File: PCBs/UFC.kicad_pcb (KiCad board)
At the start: 2 copper layers, 184.1 x 108 mm, 71 parts, among them J10 Conn_01x08_Male, J11 Conn_01x09_Male, J12 Conn_01x08_Male, J13 Conn_01x09_Male, J3 Power, J5 Matrix, J7 Driver output 2, J9 Conn_01x30_Male, SW1 SW_SPST, SW10 SW_SPST, SW11 SW_SPST, SW12 SW_SPST, SW13 SW_SPST, SW14 SW_SPST, SW15 SW_SPST, SW16 SW_SPST, SW17 SW_SPST, SW2 SW_SPST, SW3 SW_SPST, SW4 SW_SPST, SW5 SW_SPST, SW6 SW_SPST, SW7 SW_SPST, SW8 SW_SPST, SW9 SW_SPST

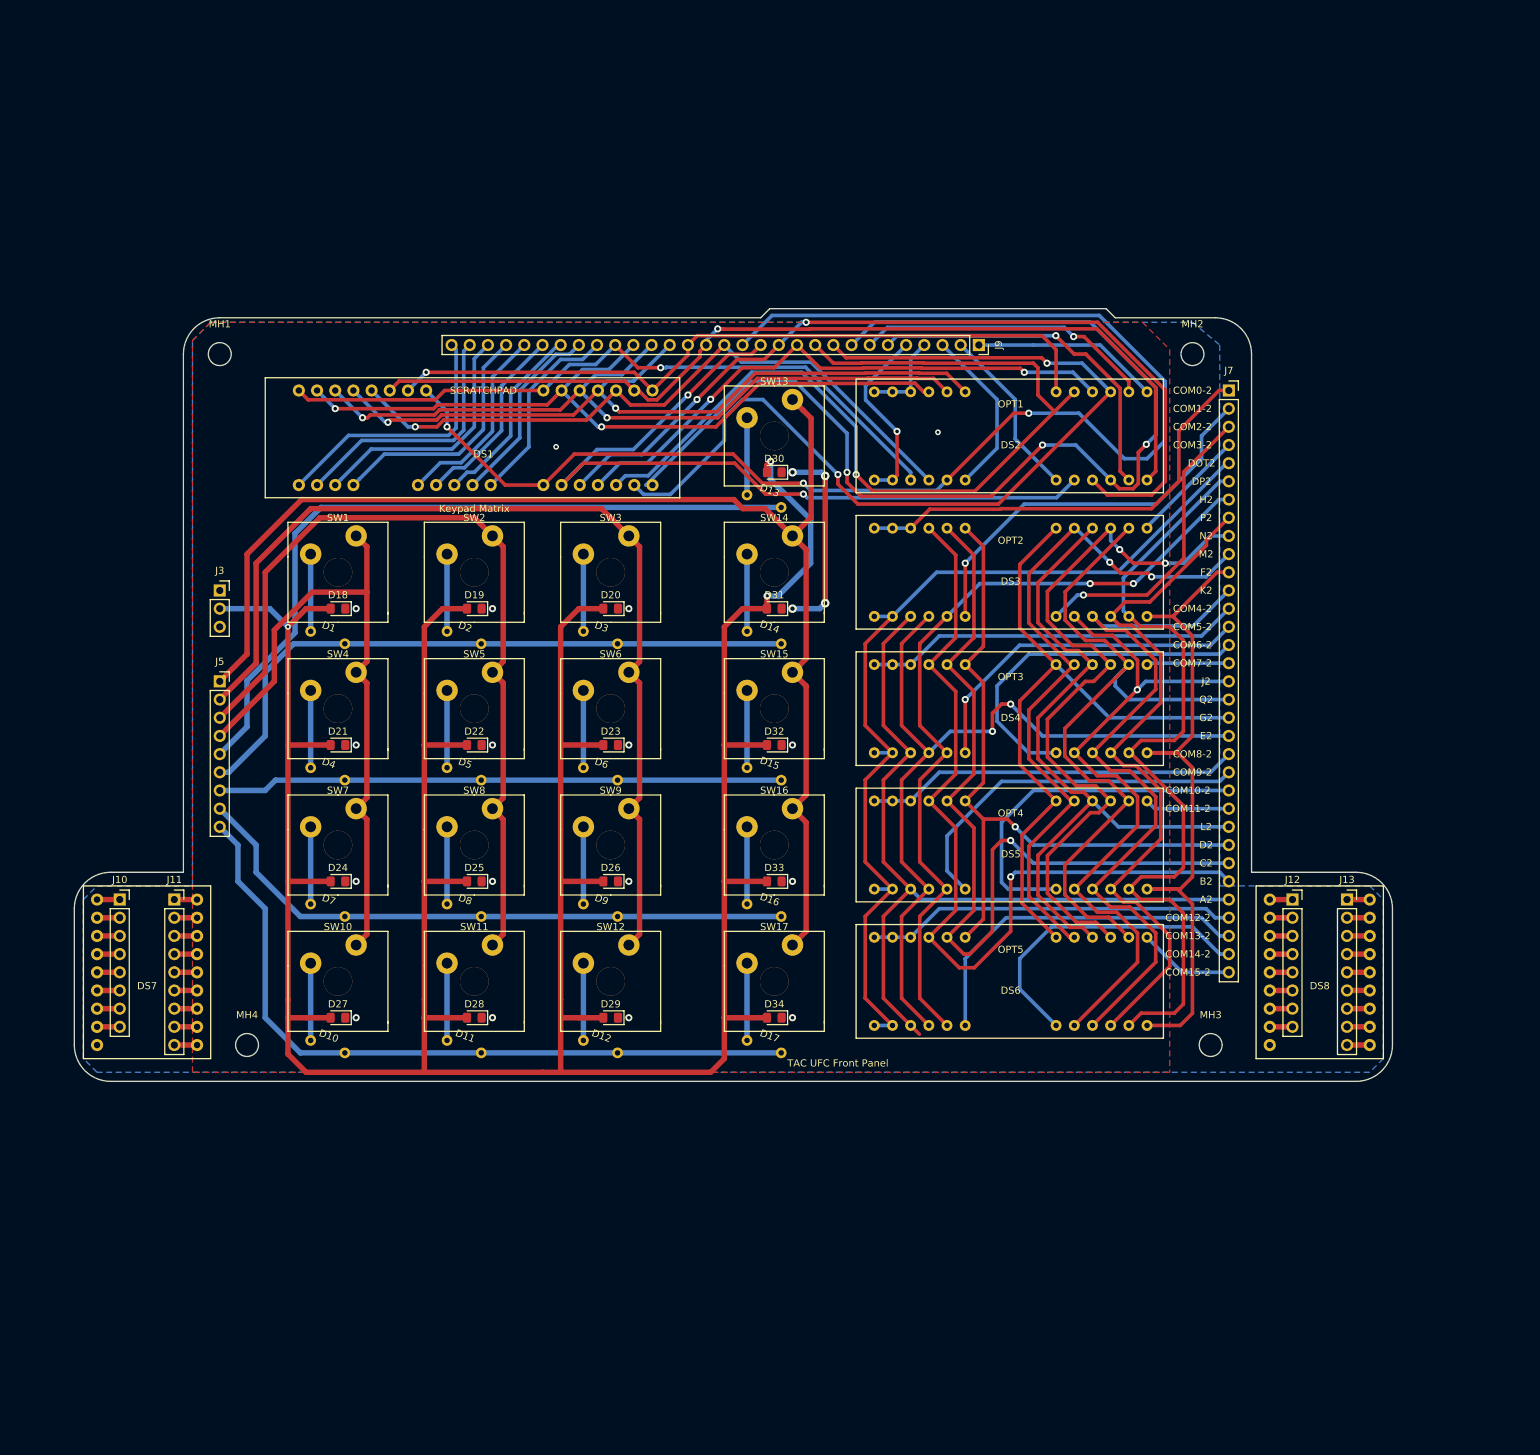
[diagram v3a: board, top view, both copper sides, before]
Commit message: Removed comm displays from PCB
Since they will be connected with wires anyways it didn't make sense to keep them on.
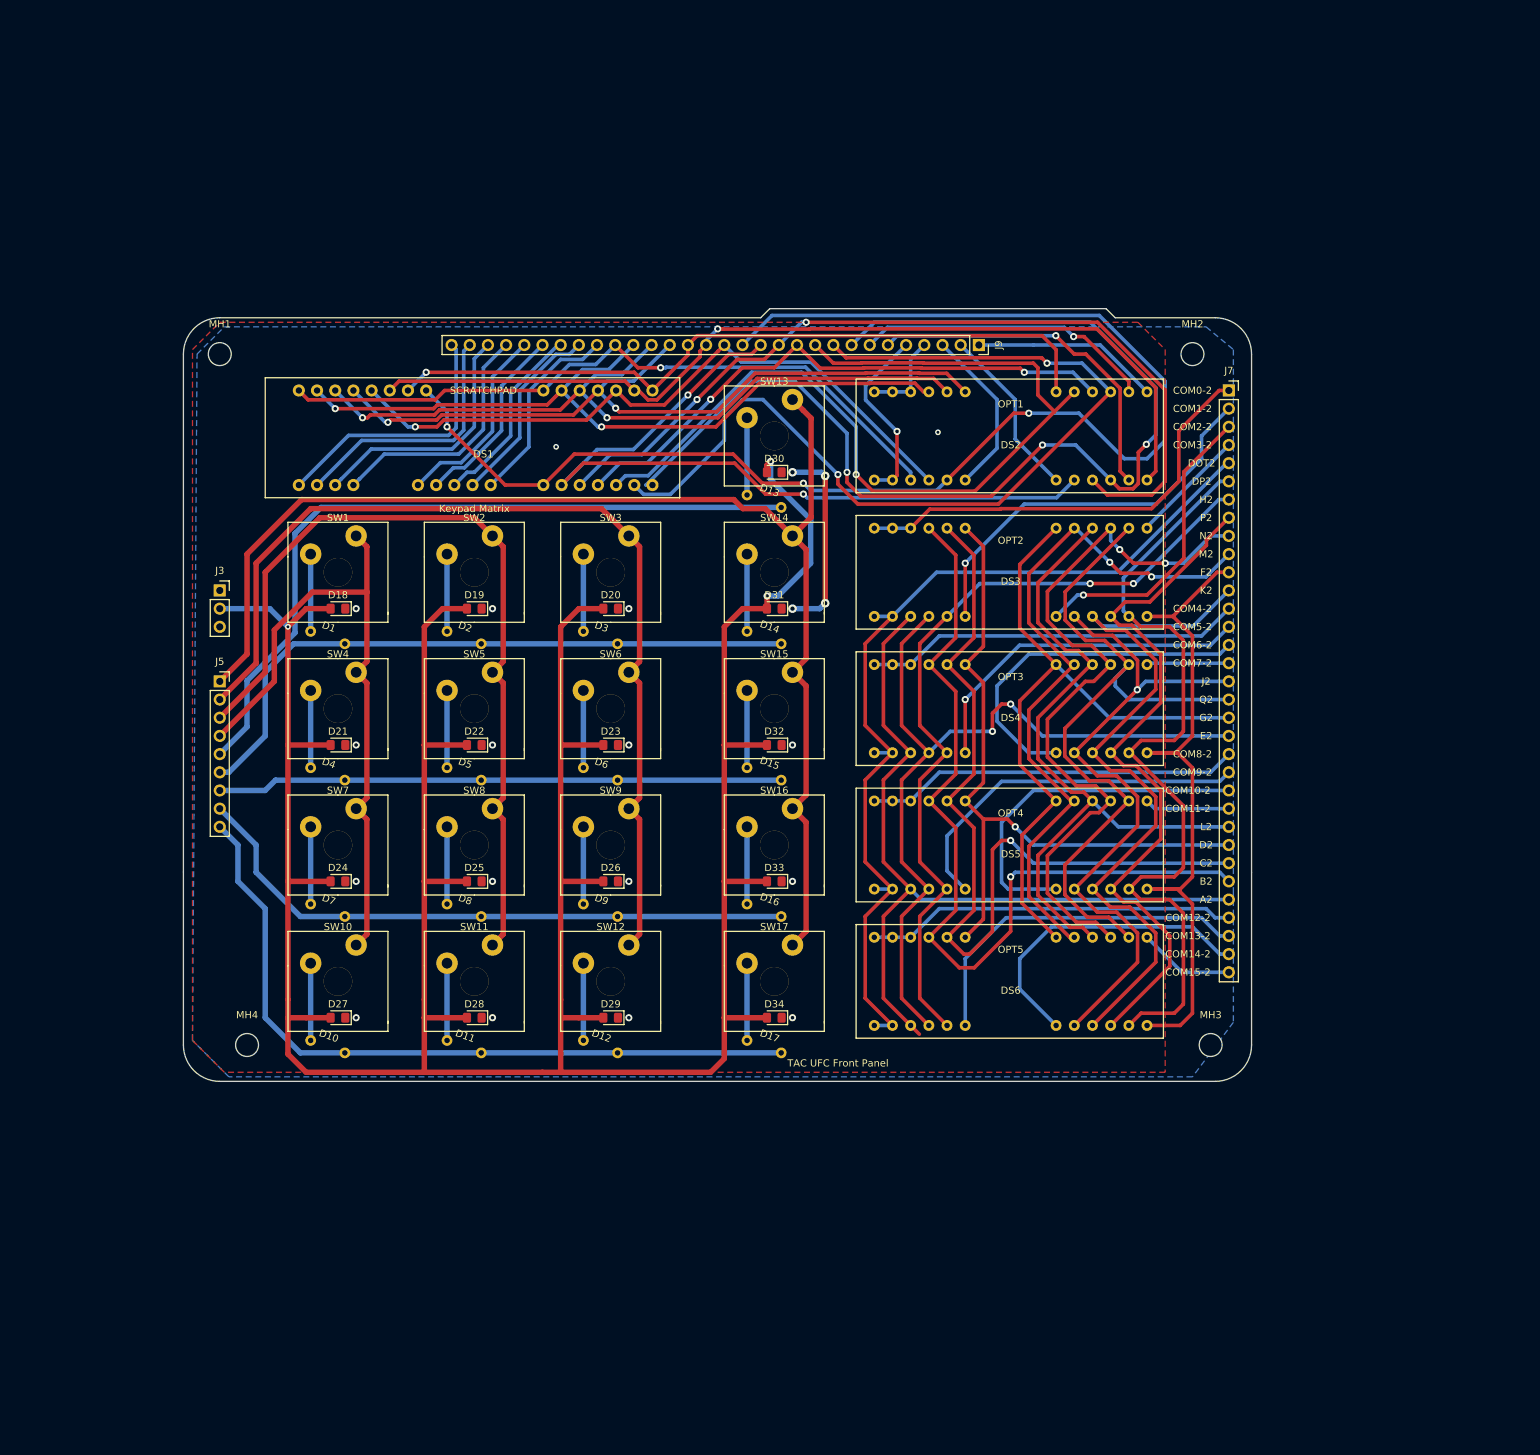
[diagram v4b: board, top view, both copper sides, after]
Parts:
- removed DS7, DS8: CommDS, UFC:OHComm
- removed J10, J12: Conn_01x08_Male, Connector_PinSocket_2.54mm:PinSocket_1x08_P2.54mm_Vertical
- removed J11, J13: Conn_01x09_Male, Connector_PinSocket_2.54mm:PinSocket_1x09_P2.54mm_Vertical
- SW1, SW10, SW11, SW12, SW13, SW14, SW15, SW16, SW17, SW2, SW3, SW4, SW5, SW6, SW7, SW8, SW9: value SW_SPST -> KeySW
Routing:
- net /C1: track 112.3 -> 106.0 mm
- net /H1: track 201.2 -> 194.9 mm
- net /B1: track 111.7 -> 105.4 mm
- net /G1: track 109.7 -> 103.3 mm
- net /E1: track 100.5 -> 94.2 mm
- net /A1: track 104.0 -> 97.7 mm
- net /F1: track 136.8 -> 130.4 mm
- net /D1: track 112.8 -> 106.5 mm
- net /M1: track 133.0 -> 126.6 mm
- net /Q1: track 48.3 -> 41.9 mm
- net /P1: track 160.5 -> 154.1 mm
- net /N1: track 135.6 -> 129.2 mm
- net /L1: track 86.3 -> 80.0 mm
- net /K1: track 126.1 -> 119.7 mm
- net /J1: track 118.2 -> 111.8 mm
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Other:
- board size 184.1 x 108 mm -> 149.2 x 108 mm

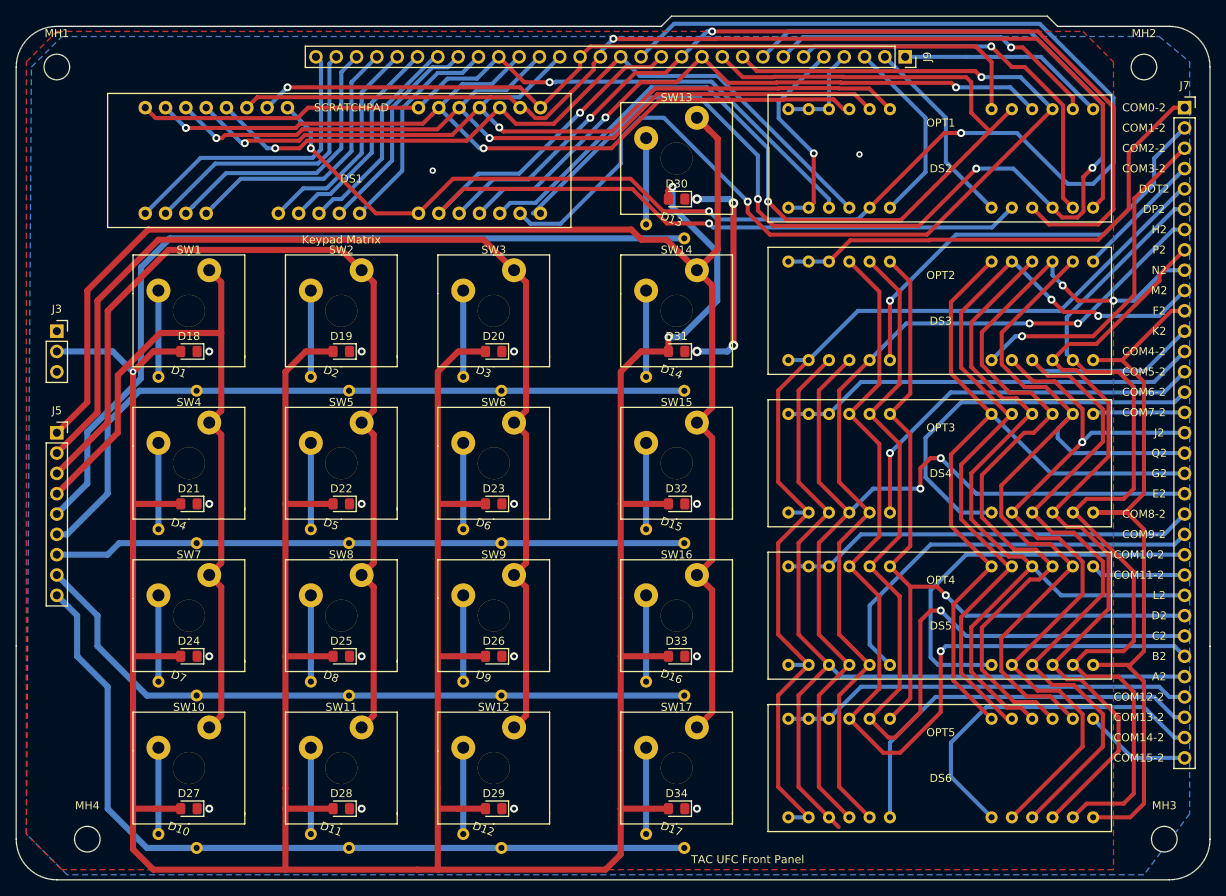
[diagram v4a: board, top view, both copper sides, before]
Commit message: Added more space for connector on comm display
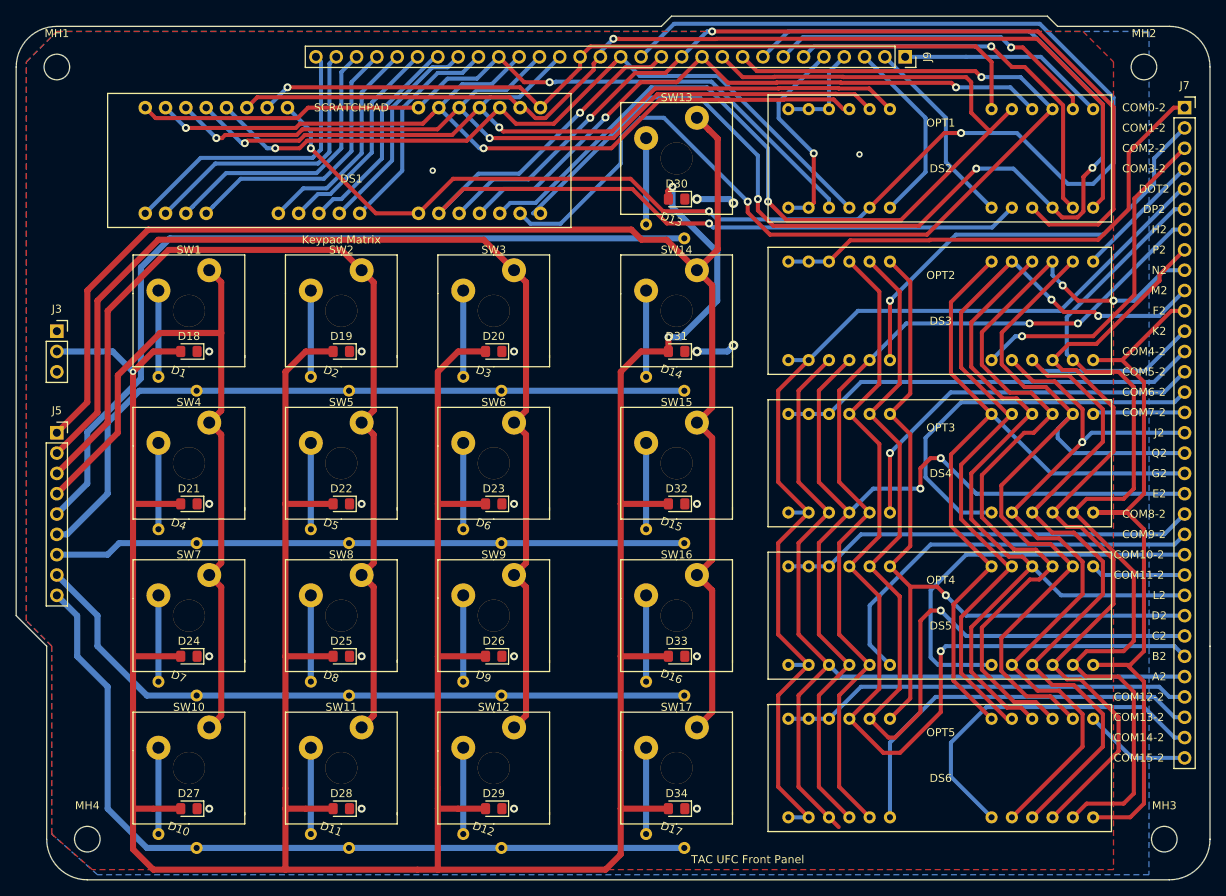
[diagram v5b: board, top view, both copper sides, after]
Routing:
- net /GND: track 27.5 -> 9.67 mm
- net /P2: track 103.0 -> 104.0 mm
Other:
- outline, holes or cut-outs redrawn

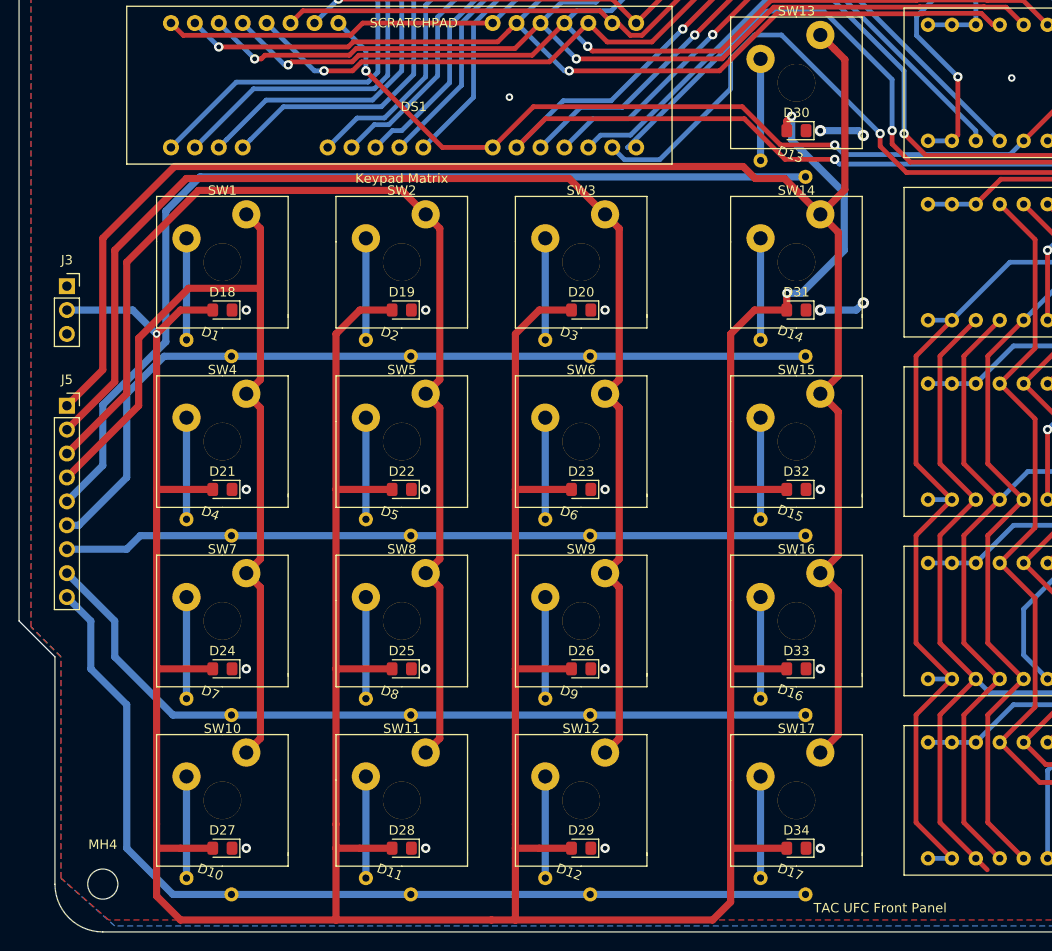
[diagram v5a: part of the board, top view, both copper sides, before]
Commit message: Fixed design error
Untested as of now.
Removed direct connection from PWM out to LEDs, as the PWM pins on the bluepill can't provide enough current. Added P channel mosfet, and individual resistors per parallel LED. For now, the single resistor for all LEDs is still present, but bypassable via jumper, for the sake of backwards compatibility.
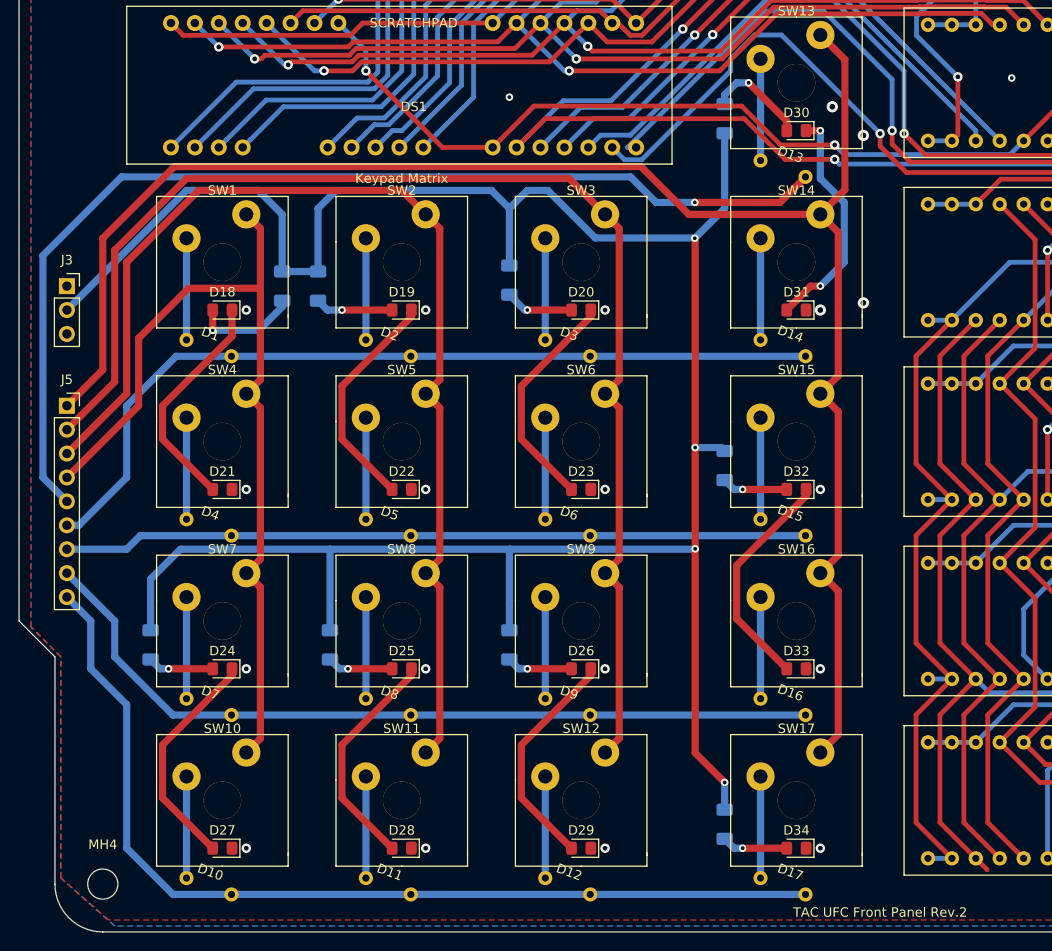
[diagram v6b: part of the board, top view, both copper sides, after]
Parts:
- added R37: 100R, Resistor_SMD:R_1206_3216Metric_Pad1.30x1.75mm_HandSolder, B.Cu at (97.8, 85.1)
- added R38: 100R, Resistor_SMD:R_1206_3216Metric_Pad1.30x1.75mm_HandSolder, B.Cu at (101.6, 85.1)
- added R39: 100R, Resistor_SMD:R_1206_3216Metric_Pad1.30x1.75mm_HandSolder, B.Cu at (121.9, 84.5)
- added R40: 100R, Resistor_SMD:R_1206_3216Metric_Pad1.30x1.75mm_HandSolder, B.Cu at (83.8, 123.2)
- added R41: 100R, Resistor_SMD:R_1206_3216Metric_Pad1.30x1.75mm_HandSolder, B.Cu at (102.9, 123.2)
- added R42: 100R, Resistor_SMD:R_1206_3216Metric_Pad1.30x1.75mm_HandSolder, B.Cu at (121.9, 123.2)
- added R43: 100R, Resistor_SMD:R_1206_3216Metric_Pad1.30x1.75mm_HandSolder, B.Cu at (144.8, 67.3)
- added R44: 100R, Resistor_SMD:R_1206_3216Metric_Pad1.30x1.75mm_HandSolder, B.Cu at (144.8, 104.1)
- added R45: 300R, Resistor_SMD:R_1206_3216Metric_Pad1.30x1.75mm_HandSolder, B.Cu at (144.8, 142.2)
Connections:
- D18 pad 1: /GND -> Net-(D18-Pad1)
- D18 pad 2: /LEDPWM -> Net-(D18-Pad2)
- D19 pad 1: /GND -> Net-(D19-Pad1)
- D19 pad 2: /LEDPWM -> Net-(D19-Pad2)
- D20 pad 1: /GND -> Net-(D20-Pad1)
- D20 pad 2: /LEDPWM -> Net-(D20-Pad2)
- D21 pad 2: /LEDPWM -> Net-(D18-Pad1)
- D22 pad 2: /LEDPWM -> Net-(D19-Pad1)
- D23 pad 2: /LEDPWM -> Net-(D20-Pad1)
- D24 pad 1: /GND -> Net-(D24-Pad1)
- D24 pad 2: /LEDPWM -> Net-(D24-Pad2)
- D25 pad 1: /GND -> Net-(D25-Pad1)
- D25 pad 2: /LEDPWM -> Net-(D25-Pad2)
- D26 pad 1: /GND -> Net-(D26-Pad1)
- D26 pad 2: /LEDPWM -> Net-(D26-Pad2)
- D27 pad 2: /LEDPWM -> Net-(D24-Pad1)
- D28 pad 2: /LEDPWM -> Net-(D25-Pad1)
- D29 pad 2: /LEDPWM -> Net-(D26-Pad1)
- D30 pad 1: /GND -> Net-(D30-Pad1)
- D30 pad 2: /LEDPWM -> Net-(D30-Pad2)
- D31 pad 2: /LEDPWM -> Net-(D30-Pad1)
- D32 pad 1: /GND -> Net-(D32-Pad1)
- D32 pad 2: /LEDPWM -> Net-(D32-Pad2)
- D33 pad 2: /LEDPWM -> Net-(D32-Pad1)
- D34 pad 2: /LEDPWM -> Net-(D34-Pad2)
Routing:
- net /LEDPWM: track 445.5 -> 255.9 mm, vias 3 -> 4
- net Net-(D30-Pad1): track 0.00 -> 24.7 mm, vias 0 -> 2
- net Net-(D19-Pad1): track 0.00 -> 24.3 mm
- net Net-(D18-Pad1): track 0.00 -> 24.3 mm
- net Net-(D25-Pad1): track 0.00 -> 24.3 mm
- net Net-(D24-Pad1): track 0.00 -> 24.3 mm
- net Net-(D20-Pad1): track 0.00 -> 24.3 mm
- net Net-(D26-Pad1): track 0.00 -> 24.3 mm
- net Net-(D32-Pad1): track 0.00 -> 24.3 mm
- net Net-(D18-Pad2): track 0.00 -> 11.2 mm, vias 0 -> 1
- net Net-(D30-Pad2): track 0.00 -> 10.8 mm, vias 0 -> 1
- net /GND: track 9.67 -> 0.00 mm
- net /ROW0: track 104.6 -> 113.8 mm, vias 0 -> 1
- net Net-(D19-Pad2): track 0.00 -> 8.28 mm, vias 0 -> 1
- net Net-(D20-Pad2): track 0.00 -> 7.27 mm, vias 0 -> 1
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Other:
- board text added: "TAC UFC Front Panel Rev.2"
- board text removed: "TAC UFC Front Panel"
